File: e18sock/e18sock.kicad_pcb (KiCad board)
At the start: 2 copper layers, 40.6 x 33 mm, 3 parts

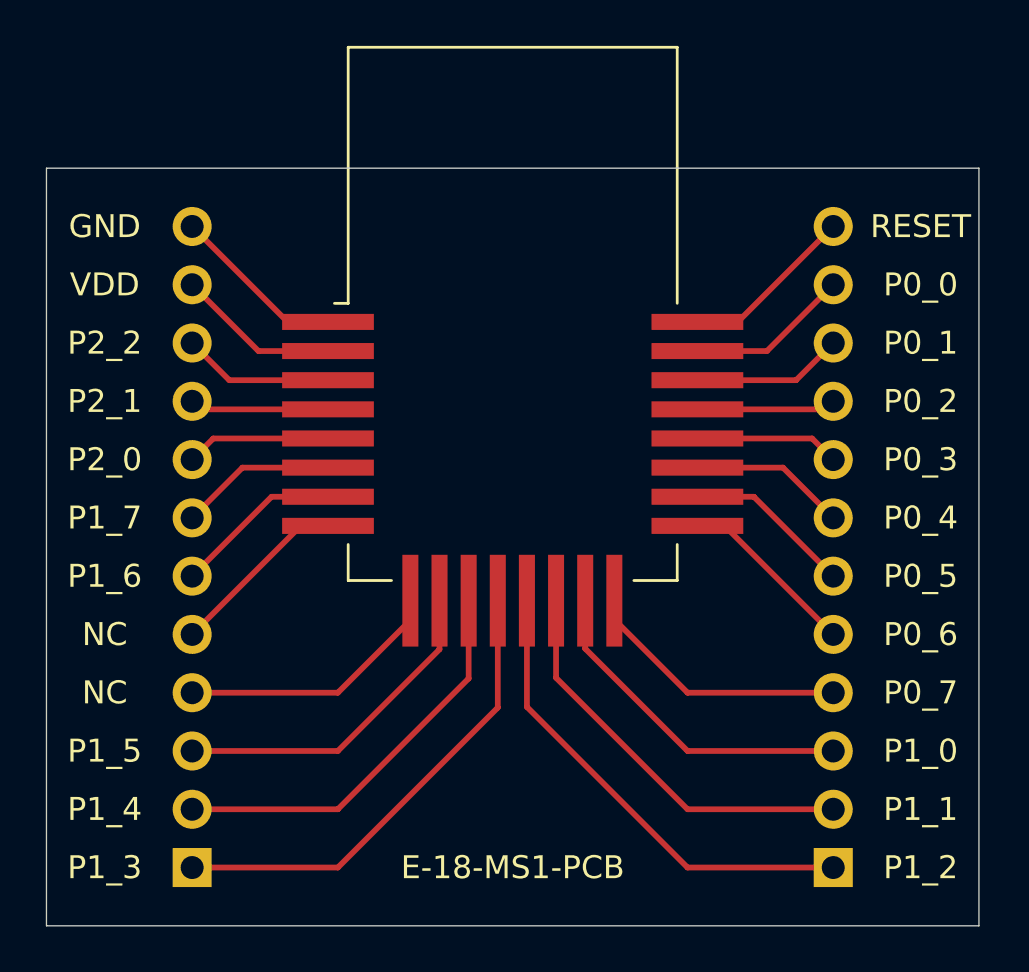
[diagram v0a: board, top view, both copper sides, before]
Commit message: Make fit for breadboards
max spacing: 10x0.1" so that 1 pin is open on each side
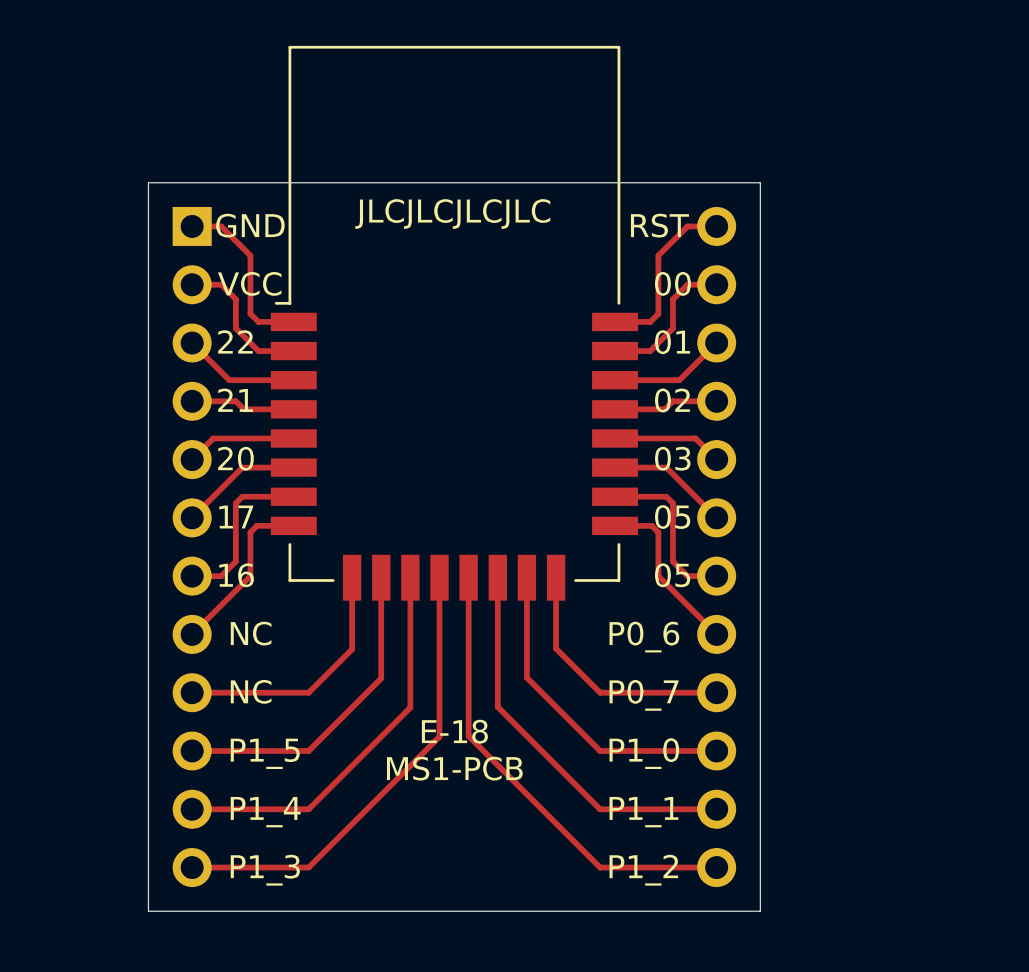
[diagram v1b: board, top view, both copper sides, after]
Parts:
- moved   5.08 mm to (139.7, 63.5)
- moved E-18-MS1-PCB 2.54 mm to (128.3, 39.4)
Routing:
- net (no net): track 265.7 -> 221.2 mm
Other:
- board size 40.6 x 33 mm -> 26.7 x 31.8 mm
- board text added: "00"
- board text added: "01"
- board text added: "02"
- board text added: "03"
- board text added: "05"
- board text added: "16"
- board text added: "17"
- board text added: "20"
- board text added: "21"
- board text added: "22"
- board text added: "E-18 MS1-PCB"
- board text added: "JLCJLCJLCJLC"
- board text added: "RST"
- board text added: "VCC"
- board text removed: "P0_0"
- board text removed: "P0_1"
- board text removed: "P0_2"
- board text removed: "P0_3"
- board text removed: "P0_4"
- board text removed: "P0_5"
- board text removed: "P1_6"
- board text removed: "P1_7"
- board text removed: "P2_0"
- board text removed: "P2_1"
- board text removed: "P2_2"
- board text removed: "RESET"
- board text removed: "VDD"
